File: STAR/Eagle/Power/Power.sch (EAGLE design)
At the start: 51 parts, among them J1 J30J-25, U1 LMR16020, U2 LMR16020, U3 LMR16020

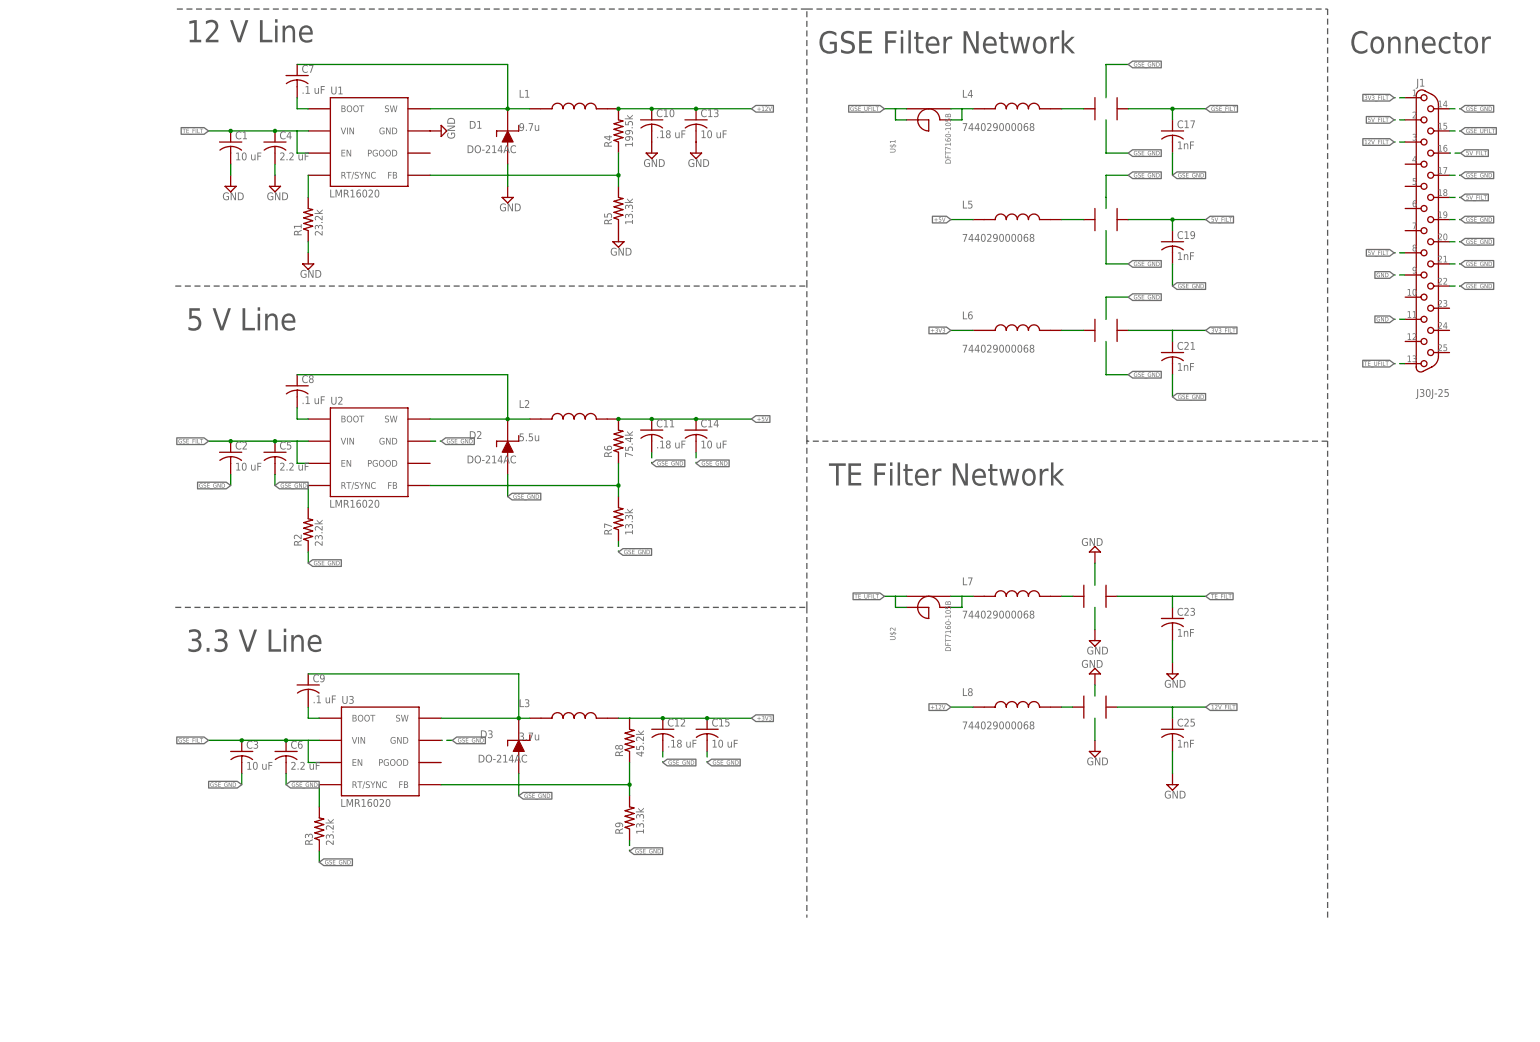
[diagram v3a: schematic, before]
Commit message: fixed choke routing on power board
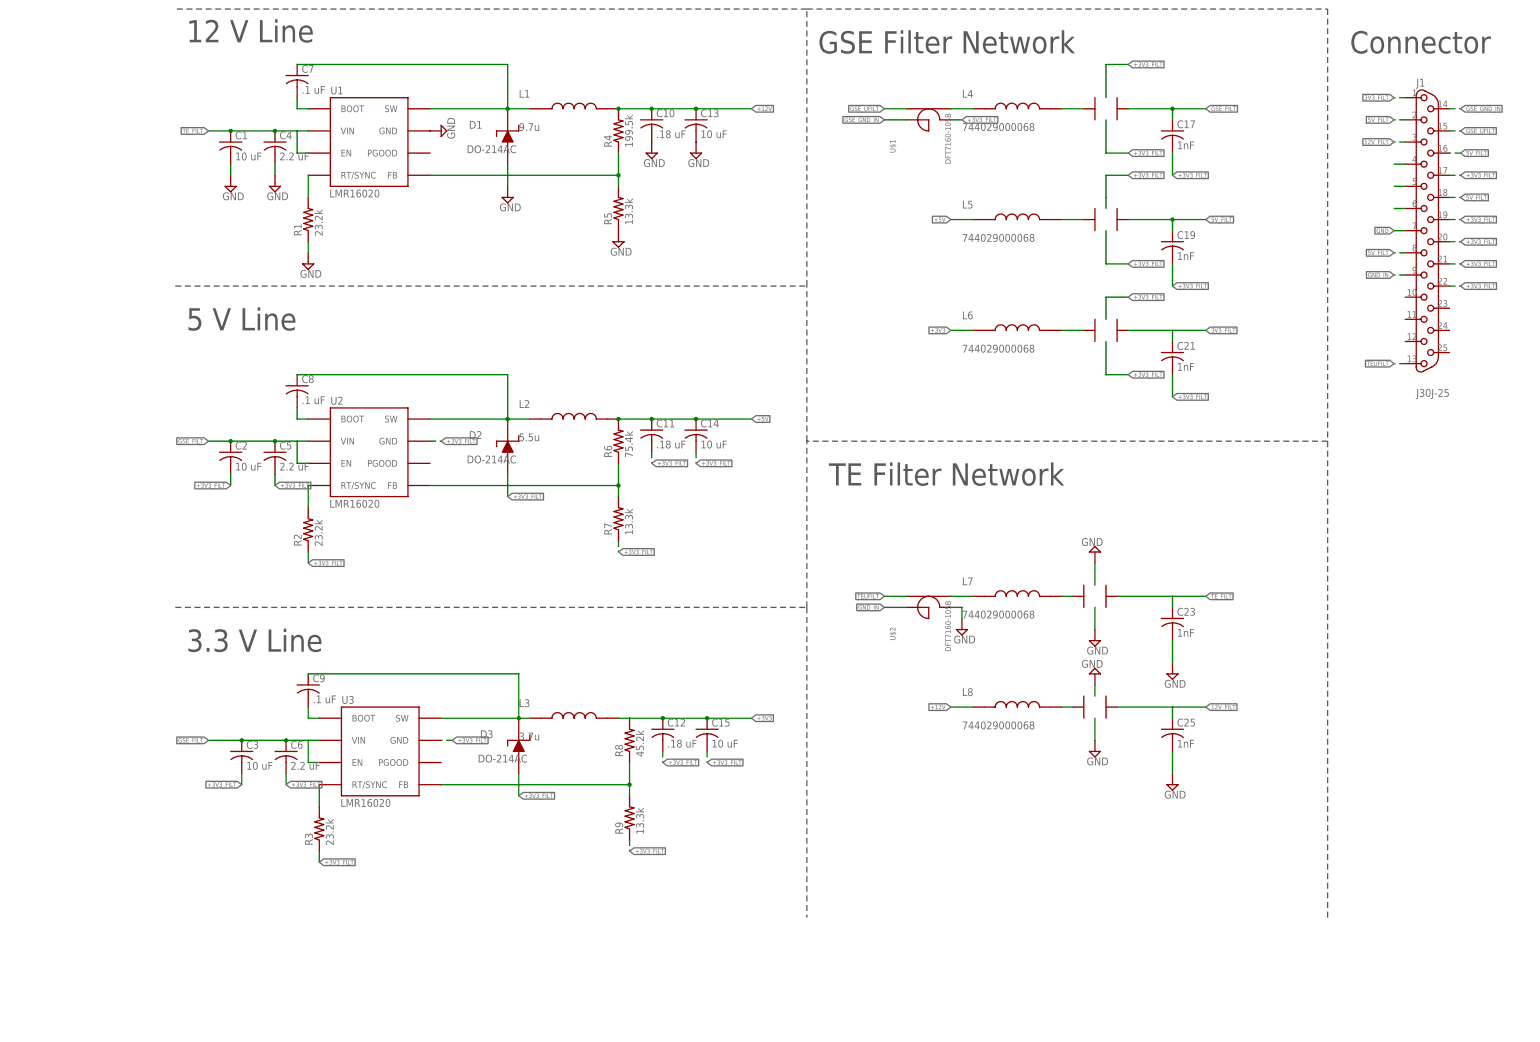
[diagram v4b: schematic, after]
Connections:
- removed net GSE_GND: C11.2, C12.2, C14.2, C15.2, C17.2, C19.2, C2.2, C21.2, C3.2, C5.2, C6.2, D2.P$1, D3.P$1, J1.14, J1.17, J1.19, J1.20, J1.21, J1.22, R2.1, R3.1, R7.1, R9.1, U$3.P$3, U$3.P$4, U$5.P$3, U$5.P$4, U2.GND, U3.GND
- removed net TE_UFILT: J1.13, U$2.P$1, U$2.P$3
- new net +3V3_FILT: C11.2, C12.2, C14.2, C15.2, C17.2, C19.2, C2.2, C21.2, C3.2, C5.2, C6.2, D2.P$1, D3.P$1, J1.17, J1.19, J1.20, J1.21, J1.22, R2.1, R3.1, R7.1, R9.1, U$1.P$2, U$3.P$3, U$3.P$4, U$5.P$3, U$5.P$4, U2.GND, U3.GND
- new net GND_IN: J1.9, U$2.P$1
- new net GSE_GND_IN: J1.14, U$1.P$1
- new net N$37: J1.6
- new net N$38: J1.5
- new net N$39: J1.4
- new net TEUFILT: J1.13, U$2.P$3
- net GND: now also J1.7, U$2.P$2; no longer J1.11, J1.9
- net GSE_UFILT: no longer U$1.P$1
- net N$28: no longer U$1.P$2
- net N$29: no longer U$2.P$2

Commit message: I think I fixed all of the GSE_GND being '+3V3_FILT' but I don't know how that happened in the first place
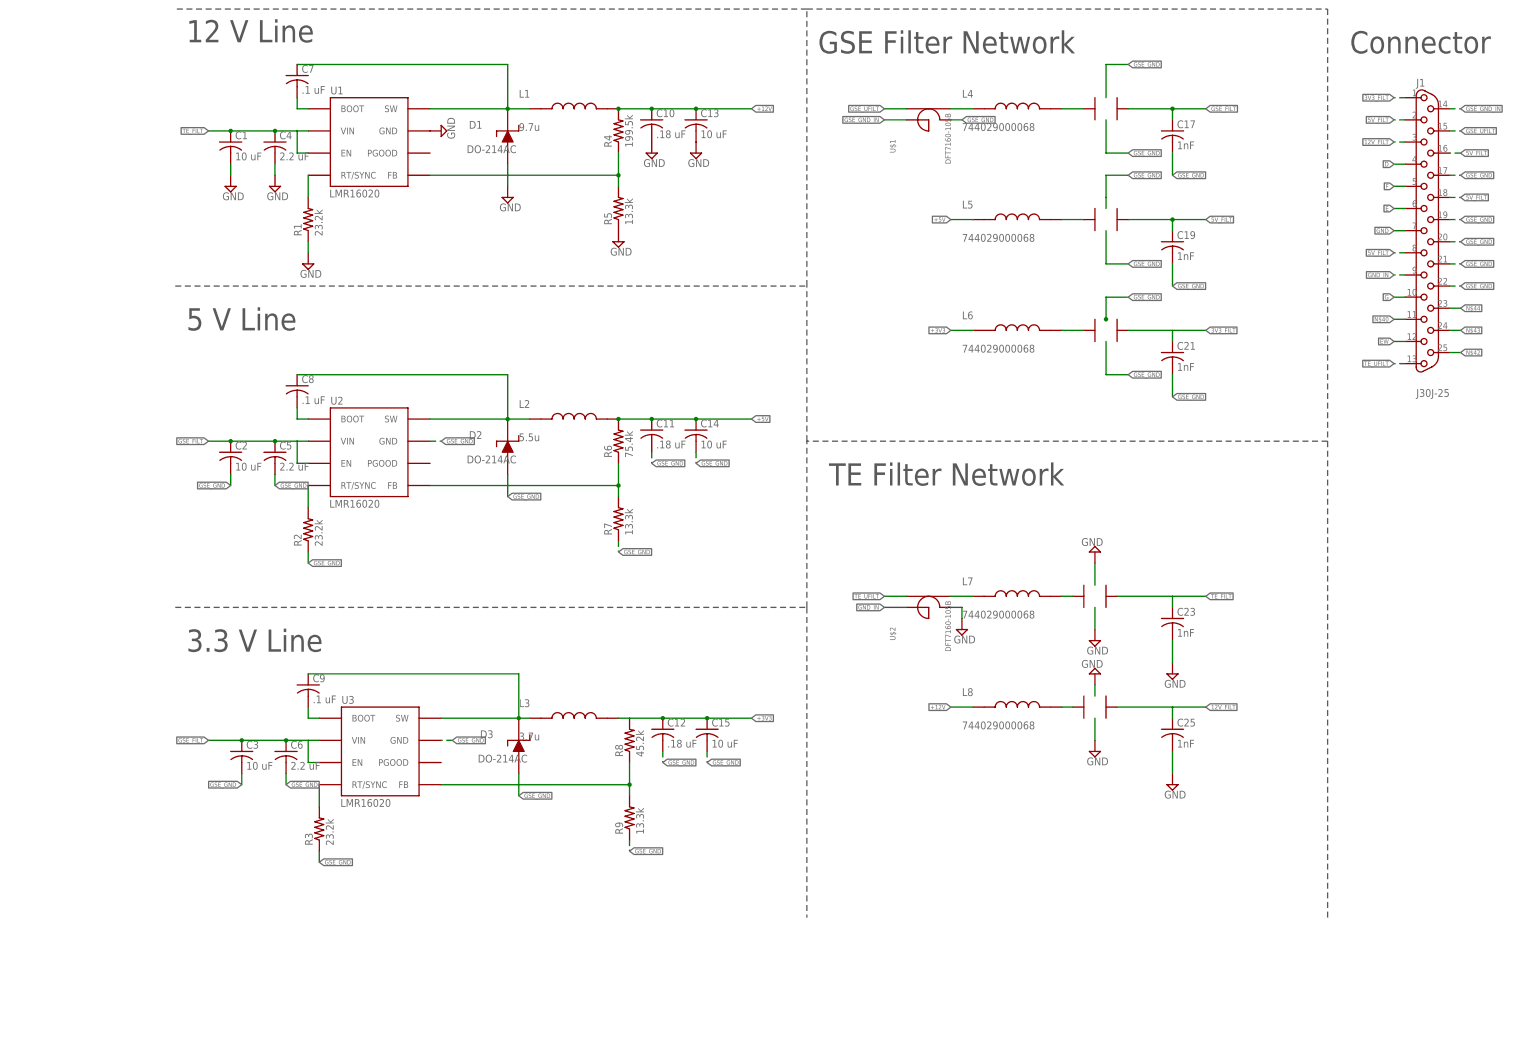
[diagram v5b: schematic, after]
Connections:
- net +3V3_FILT renamed GSE_GND
- net N$37 renamed E
- net N$38 renamed F
- net N$39 renamed D
- net TEUFILT renamed TE_UFILT
- new net EW: J1.12
- new net G: J1.10
- new net N$40: J1.11
- new net N$42: J1.25
- new net N$43: J1.24
- new net N$44: J1.23

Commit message: Fixed Blaire's  nonsense on the power board. No longer shorting 3V3 to GSE_GND. The input names still make no sense
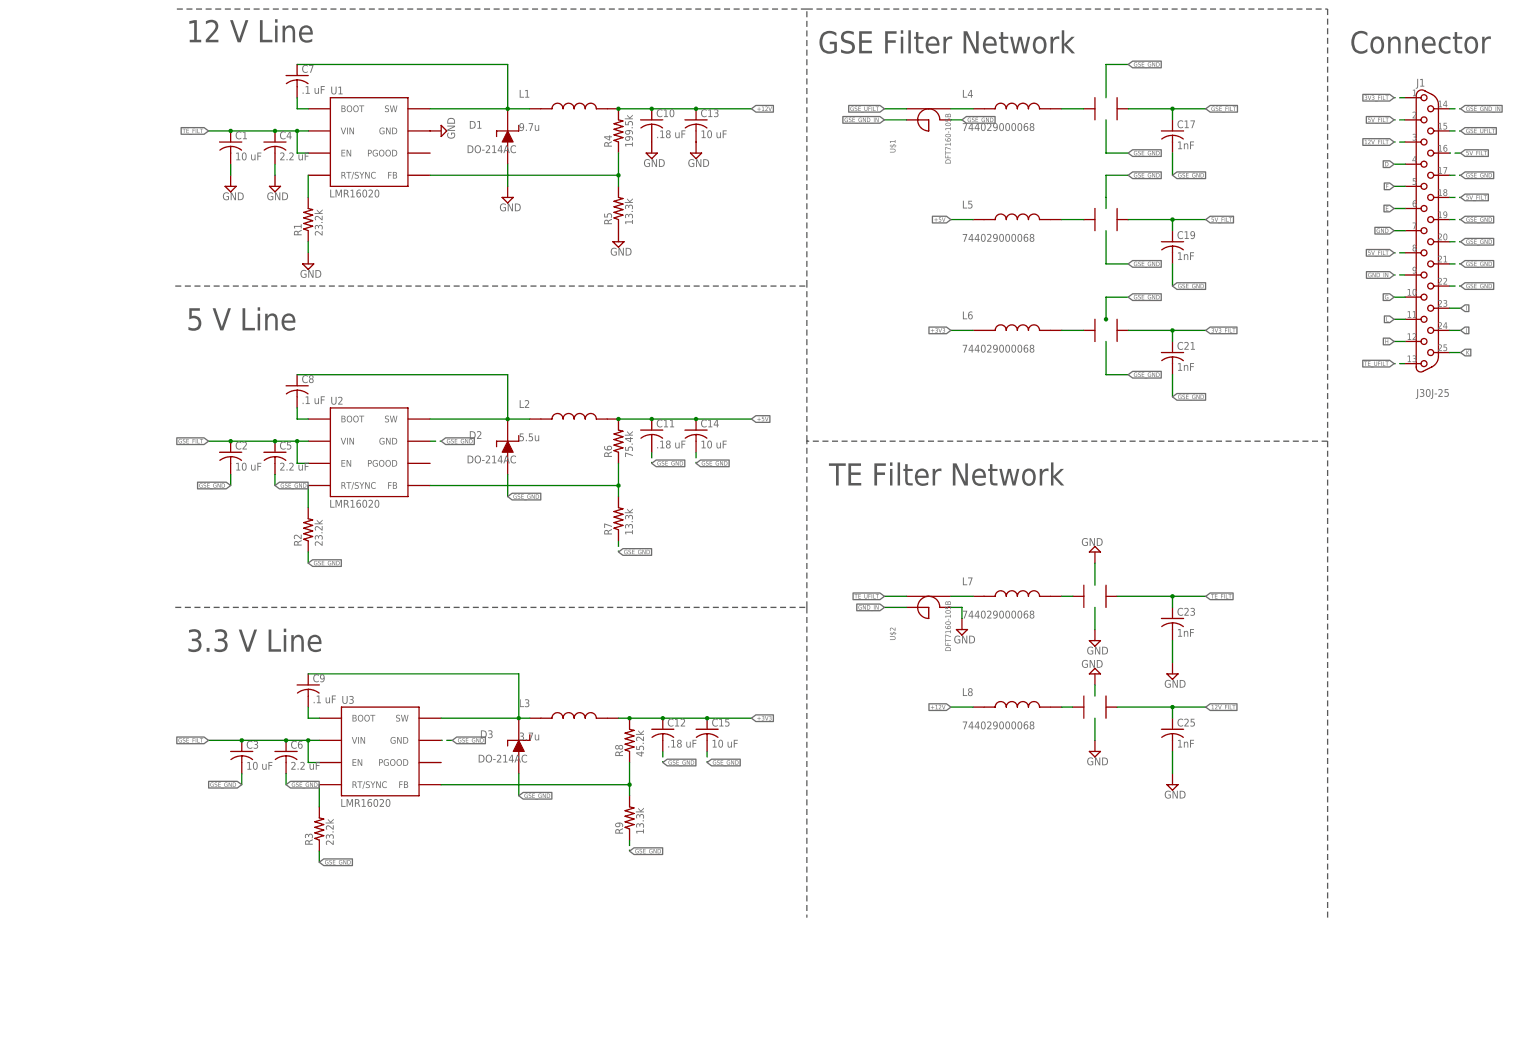
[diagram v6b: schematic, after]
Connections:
- net EW renamed H
- net N$40 renamed L
- net N$42 renamed K
- net N$43 renamed J
- net N$44 renamed I
- net GSE_GND: now also U$4.P$3, U$4.P$4
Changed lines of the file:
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@@
 <?xml version="1.0" encoding="utf-8"?>
 <!DOCTYPE eagle SYSTEM "eagle.dtd">
-<eagle version="7.6.0">
+<eagle version="9.1.0">
 <drawing>
 <settings>
 <setting alwaysvectorfont="no"/>
+<setting keepoldvectorfont="yes"/>
 <setting verticaltext="up"/>
 </settings>
@@
 <label x="175.26" y="111.76" size="1.016" layer="95" xref="yes"/>
 <pinref part="L3" gate="G$1" pin="P$2"/>
+<junction x="147.32" y="111.76"/>
 </segment>
 <segment>
@@
 <junction x="66.04" y="175.26"/>
 <label x="50.8" y="175.26" size="1.016" layer="95" rot="R180" xref="yes"/>
+<junction x="71.12" y="175.26"/>
 </segment>
 <segment>
@@
 <junction x="58.42" y="106.68"/>
 <label x="50.8" y="106.68" size="1.016" layer="95" rot="R180" xref="yes"/>
+<junction x="73.66" y="106.68"/>
 </segment>
 </net>
@@
 <label x="279.4" y="200.66" size="1.016" layer="95" xref="yes"/>
 <pinref part="U$5" gate="G$1" pin="P$2"/>
+<junction x="271.78" y="200.66"/>
 </segment>
 <segment>
@@
 <label x="279.4" y="139.7" size="1.016" layer="95" xref="yes"/>
 <pinref part="U$6" gate="G$1" pin="P$2"/>
+<junction x="271.78" y="139.7"/>
 </segment>
 <segment>
@@
 <junction x="66.04" y="246.38"/>
 <label x="50.8" y="246.38" size="1.016" layer="95" rot="R180" xref="yes"/>
+<junction x="71.12" y="246.38"/>
 </segment>
 </net>
@@
 <label x="279.4" y="114.3" size="1.016" layer="95" xref="yes"/>
 <pinref part="U$7" gate="G$1" pin="P$2"/>
+<junction x="271.78" y="114.3"/>
 </segment>
 <segment>
@@
 <wire x1="256.54" y1="236.22" x2="256.54" y2="231.14" width="0.1524" layer="91"/>
 <wire x1="256.54" y1="228.6" x2="256.54" y2="231.14" width="0.1524" layer="91"/>
+<pinref part="U$4" gate="G$1" pin="P$3"/>
 </segment>
 <segment>
@@
 <wire x1="256.54" y1="215.9" x2="256.54" y2="223.52" width="0.1524" layer="91"/>
 <label x="261.62" y="208.28" size="1.016" layer="95" xref="yes"/>
+<pinref part="U$4" gate="G$1" pin="P$4"/>
 </segment>
 <segment>
@@
 </segment>
 </net>
-<net name="N$40" class="0">
+<net name="L" class="0">
 <segment>
 <pinref part="J1" gate="G$1" pin="11"/>
@@
 </segment>
 </net>
-<net name="N$42" class="0">
+<net name="K" class="0">
 <segment>
 <pinref part="J1" gate="G$1" pin="25"/>
@@
 </segment>
 </net>
-<net name="N$43" class="0">
+<net name="J" class="0">
 <segment>
 <pinref part="J1" gate="G$1" pin="24"/>
@@
 </segment>
 </net>
-<net name="N$44" class="0">
+<net name="I" class="0">
 <segment>
 <pinref part="J1" gate="G$1" pin="23"/>
@@
 </segment>
 </net>
-<net name="EW" class="0">
+<net name="H" class="0">
 <segment>
 <pinref part="J1" gate="G$1" pin="12"/>
